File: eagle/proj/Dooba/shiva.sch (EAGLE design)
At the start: 112 parts, among them J1 DM3D-SFDM, J2 USB-BAMPHENOL-MICRO, J3 SJ1-3523N, J4 ADAFRUIT_OLED_13, SW1 LEFT, SW2 UP, SW3 CENTER, SW4 DOWN, SW5 RIGHT, SW6 VOL_UP, SW7 VOL_DN, U1 STM32F030X-LQFP48LQFP48, U10 CS4334, U11 LM4811PDSO-10, U12 5.0V, U13 MCP23008QFN, U2 TPS61200S-PVSON-N10, U3 MAX1811SO8, U4 FT232RQFN32, U5 SN74LVC1G125SOT23-5, U6 SN74LVC1G125SOT23-5, U7 3.3V, U8 3.3V, U9 STA013LQFP44, X1 16MHz, X2 14.7456MHz

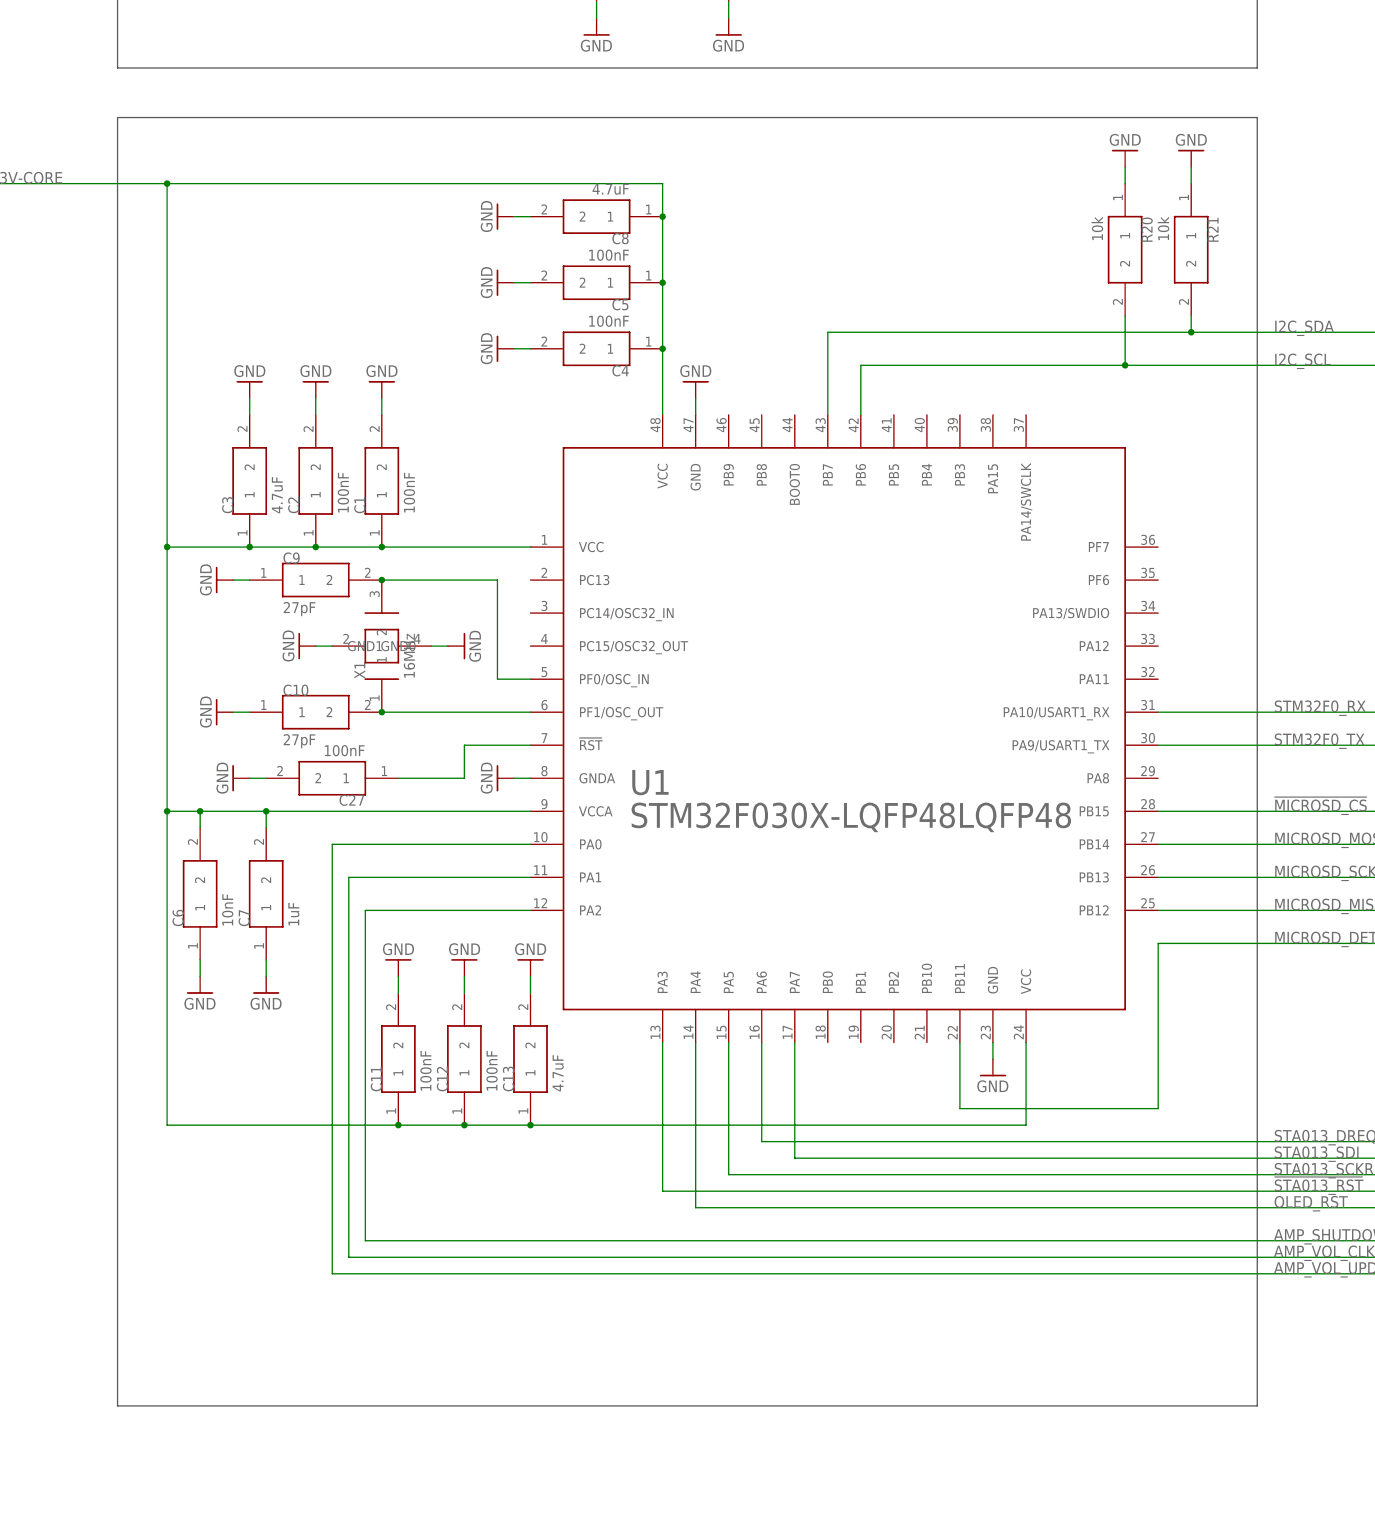
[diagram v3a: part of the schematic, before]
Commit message: Finished designing Shiva MP3 Player Schematic
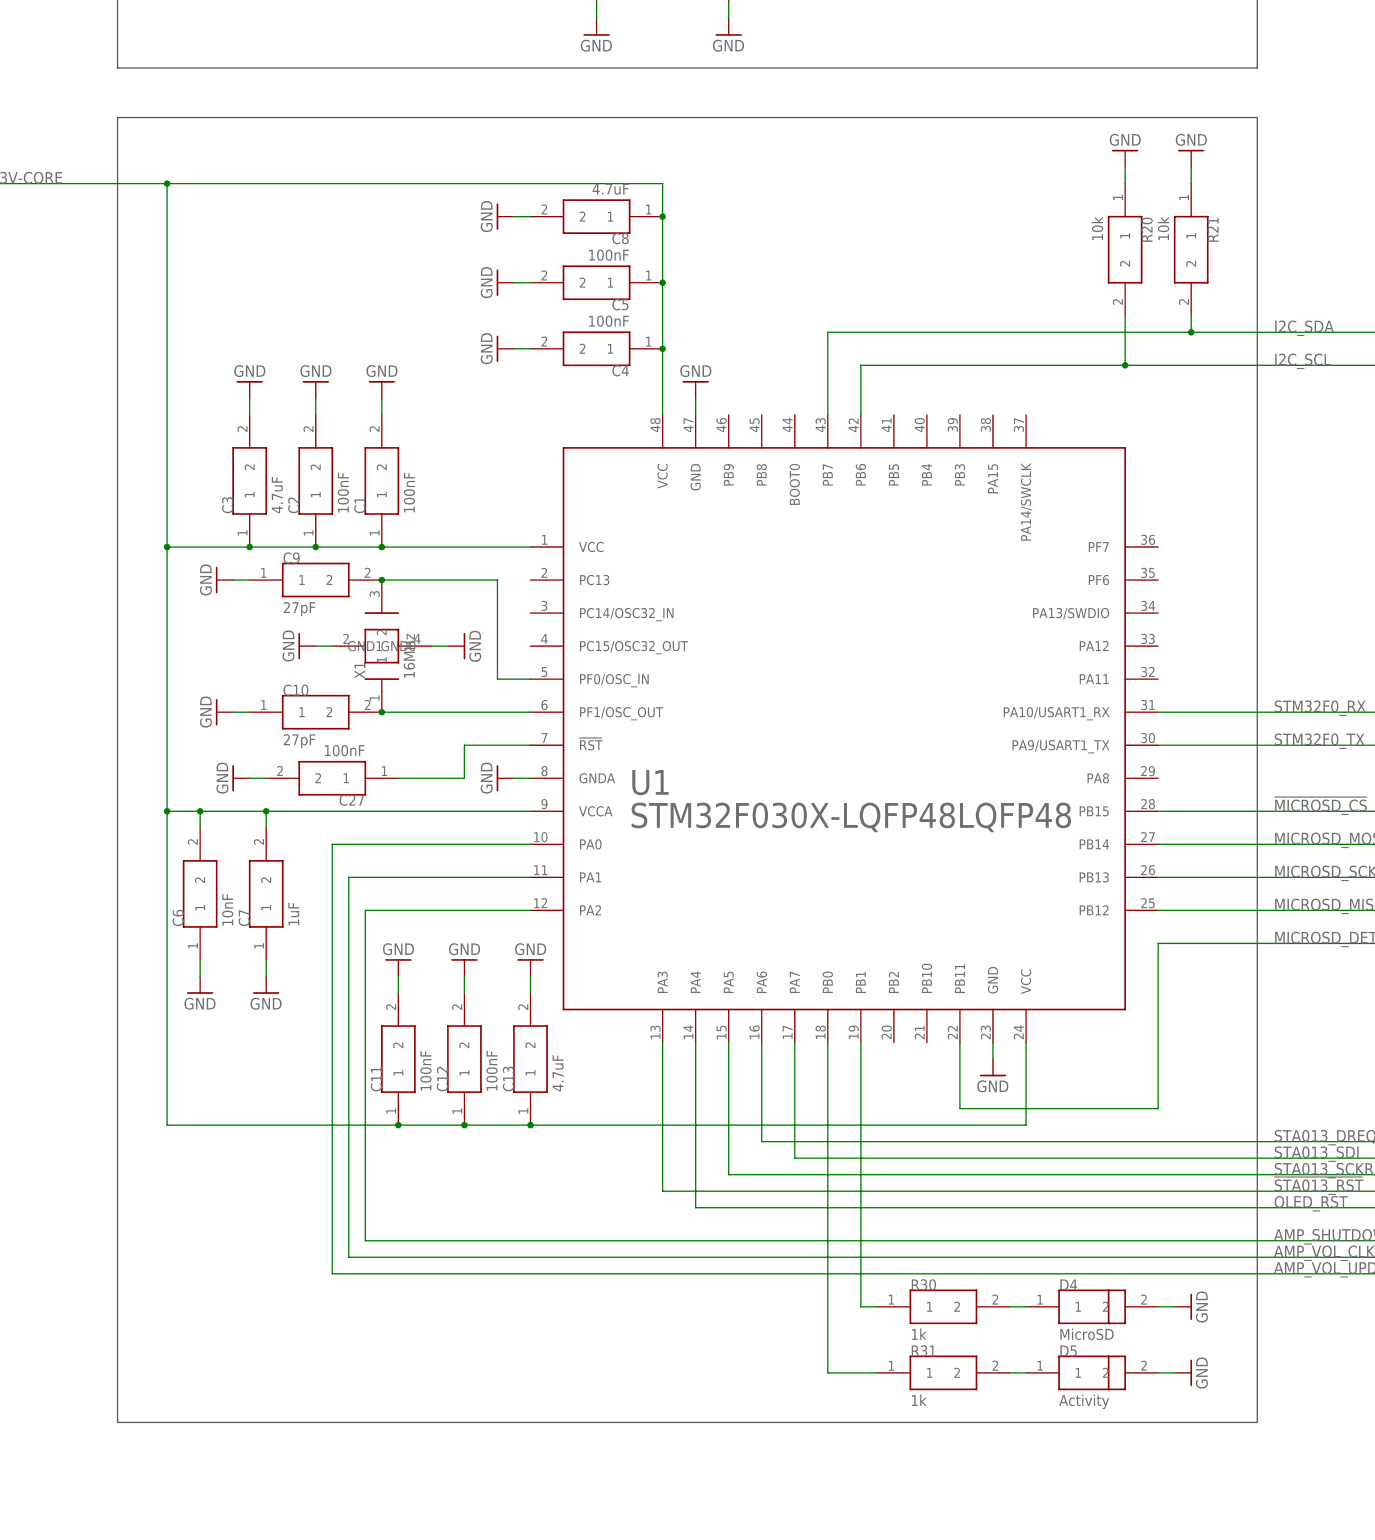
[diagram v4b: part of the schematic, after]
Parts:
- added D4: MicroSD, dooba:LED0805
- added D5: Activity, dooba:LED0805
- added R30, R31: 1k, dooba:RES0805
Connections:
- new net N$43: D4.1, R30.2
- new net N$44: D5.1, R31.2
- new net N$45: R30.1, U1.PB1
- new net N$46: R31.1, U1.PB0
- net GND: now also D4.2, D5.2
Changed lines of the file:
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@@
 <part name="GND104" library="supply1" deviceset="GND" device=""/>
 <part name="GND105" library="supply1" deviceset="GND" device=""/>
+<part name="R30" library="dooba" deviceset="RES" device="0805" value="1k"/>
+<part name="R31" library="dooba" deviceset="RES" device="0805" value="1k"/>
+<part name="D4" library="dooba" deviceset="LED" device="0805" value="MicroSD"/>
+<part name="D5" library="dooba" deviceset="LED" device="0805" value="Activity"/>
+<part name="GND106" library="supply1" deviceset="GND" device=""/>
+<part name="GND107" library="supply1" deviceset="GND" device=""/>
 </parts>
 <sheets>
@@
 <text x="441.96" y="741.68" size="1.778" layer="97">USB UART Circuit
 Provides USB Serial Interface</text>
-<wire x1="881.38" y1="675.64" x2="881.38" y2="477.52" width="0.1524" layer="97"/>
-<wire x1="881.38" y1="477.52" x2="706.12" y2="477.52" width="0.1524" layer="97"/>
-<wire x1="706.12" y1="477.52" x2="706.12" y2="675.64" width="0.1524" layer="97"/>
+<wire x1="881.38" y1="675.64" x2="881.38" y2="474.98" width="0.1524" layer="97"/>
+<wire x1="881.38" y1="474.98" x2="706.12" y2="474.98" width="0.1524" layer="97"/>
+<wire x1="706.12" y1="474.98" x2="706.12" y2="675.64" width="0.1524" layer="97"/>
 <wire x1="706.12" y1="675.64" x2="881.38" y2="675.64" width="0.1524" layer="97"/>
 <wire x1="1168.4" y1="853.44" x2="1168.4" y2="754.38" width="0.1524" layer="97"/>
@@
 <instance part="GND104" gate="1" x="985.52" y="622.3" rot="R270"/>
 <instance part="GND105" gate="1" x="985.52" y="617.22" rot="R270"/>
+<instance part="R30" gate="R1" x="833.12" y="492.76"/>
+<instance part="R31" gate="R1" x="833.12" y="482.6"/>
+<instance part="D4" gate="D1" x="855.98" y="492.76"/>
+<instance part="D5" gate="D1" x="855.98" y="482.6"/>
+<instance part="GND106" gate="1" x="871.22" y="492.76" rot="R90"/>
+<instance part="GND107" gate="1" x="871.22" y="482.6" rot="R90"/>
 </instances>
 <busses>
@@
 <pinref part="GND105" gate="1" pin="GND"/>
 <wire x1="990.6" y1="617.22" x2="988.06" y2="617.22" width="0.1524" layer="91"/>
+</segment>
+<segment>
+<pinref part="D4" gate="D1" pin="2"/>
+<pinref part="GND106" gate="1" pin="GND"/>
+<wire x1="866.14" y1="492.76" x2="868.68" y2="492.76" width="0.1524" layer="91"/>
+</segment>
+<segment>
+<pinref part="D5" gate="D1" pin="2"/>
+<pinref part="GND107" gate="1" pin="GND"/>
+<wire x1="866.14" y1="482.6" x2="868.68" y2="482.6" width="0.1524" layer="91"/>
 </segment>
 </net>
@@
 </segment>
 </net>
+<net name="N$43" class="0">
+<segment>
+<pinref part="R30" gate="R1" pin="2"/>
+<pinref part="D4" gate="D1" pin="1"/>
+<wire x1="843.28" y1="492.76" x2="845.82" y2="492.76" width="0.1524" layer="91"/>
+</segment>
+</net>
+<net name="N$44" class="0">
+<segment>
+<pinref part="R31" gate="R1" pin="2"/>
+<pinref part="D5" gate="D1" pin="1"/>
+<wire x1="843.28" y1="482.6" x2="845.82" y2="482.6" width="0.1524" layer="91"/>
+</segment>
+</net>
+<net name="N$45" class="0">
+<segment>
+<pinref part="U1" gate="U1" pin="PB1"/>
+<pinref part="R30" gate="R1" pin="1"/>
+<wire x1="820.42" y1="533.4" x2="820.42" y2="492.76" width="0.1524" layer="91"/>
+<wire x1="820.42" y1="492.76" x2="822.96" y2="492.76" width="0.1524" layer="91"/>
+</segment>
+</net>
+<net name="N$46" class="0">
+<segment>
+<pinref part="U1" gate="U1" pin="PB0"/>
+<pinref part="R31" gate="R1" pin="1"/>
+<wire x1="815.34" y1="533.4" x2="815.34" y2="482.6" width="0.1524" layer="91"/>
+<wire x1="815.34" y1="482.6" x2="822.96" y2="482.6" width="0.1524" layer="91"/>
+</segment>
+</net>
